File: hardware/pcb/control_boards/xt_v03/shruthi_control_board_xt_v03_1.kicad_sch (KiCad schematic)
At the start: 29 parts, among them IC1 24LC512, IC10 ATMEGA644p, J1 M06SIP, J2 POWER, J3 M03PTH, J4 POWER, Q1 20MHz, U1 AVRISP, X1 MIDI, X2 MIDI

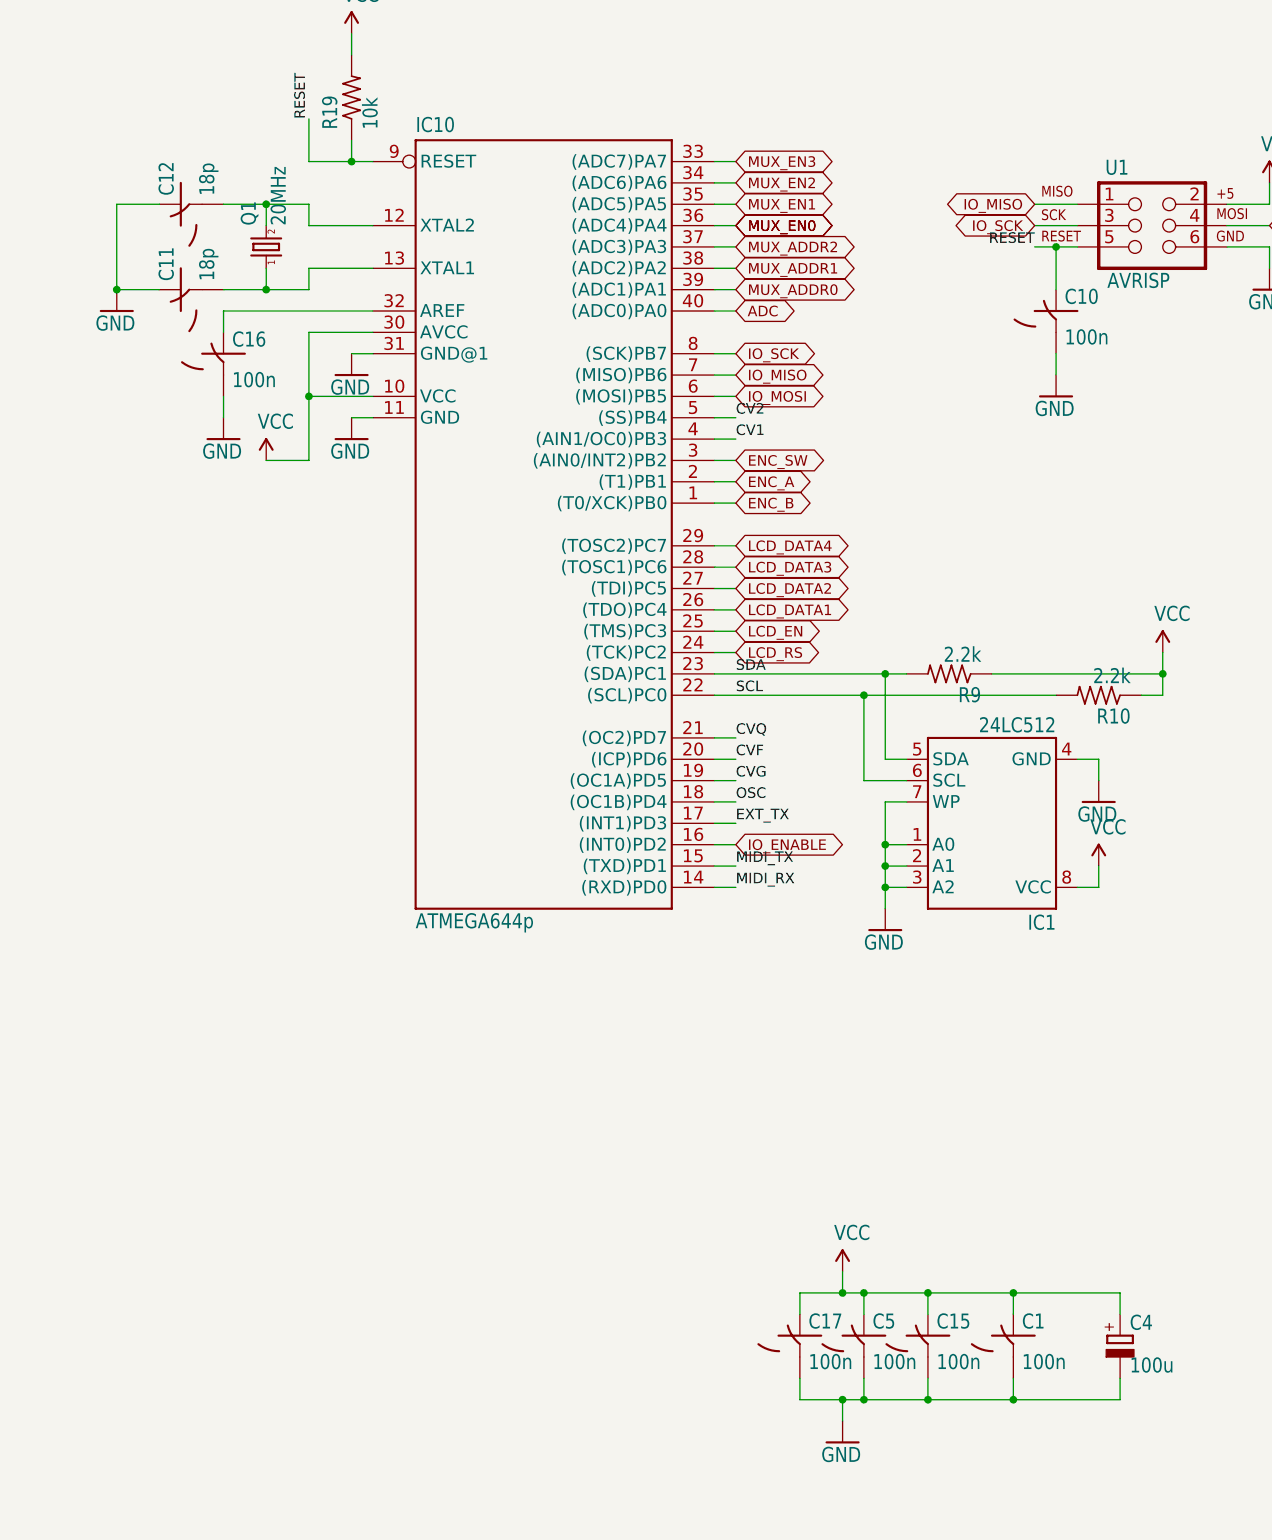
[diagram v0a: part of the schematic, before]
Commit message: update capacitors to use kicad symbols
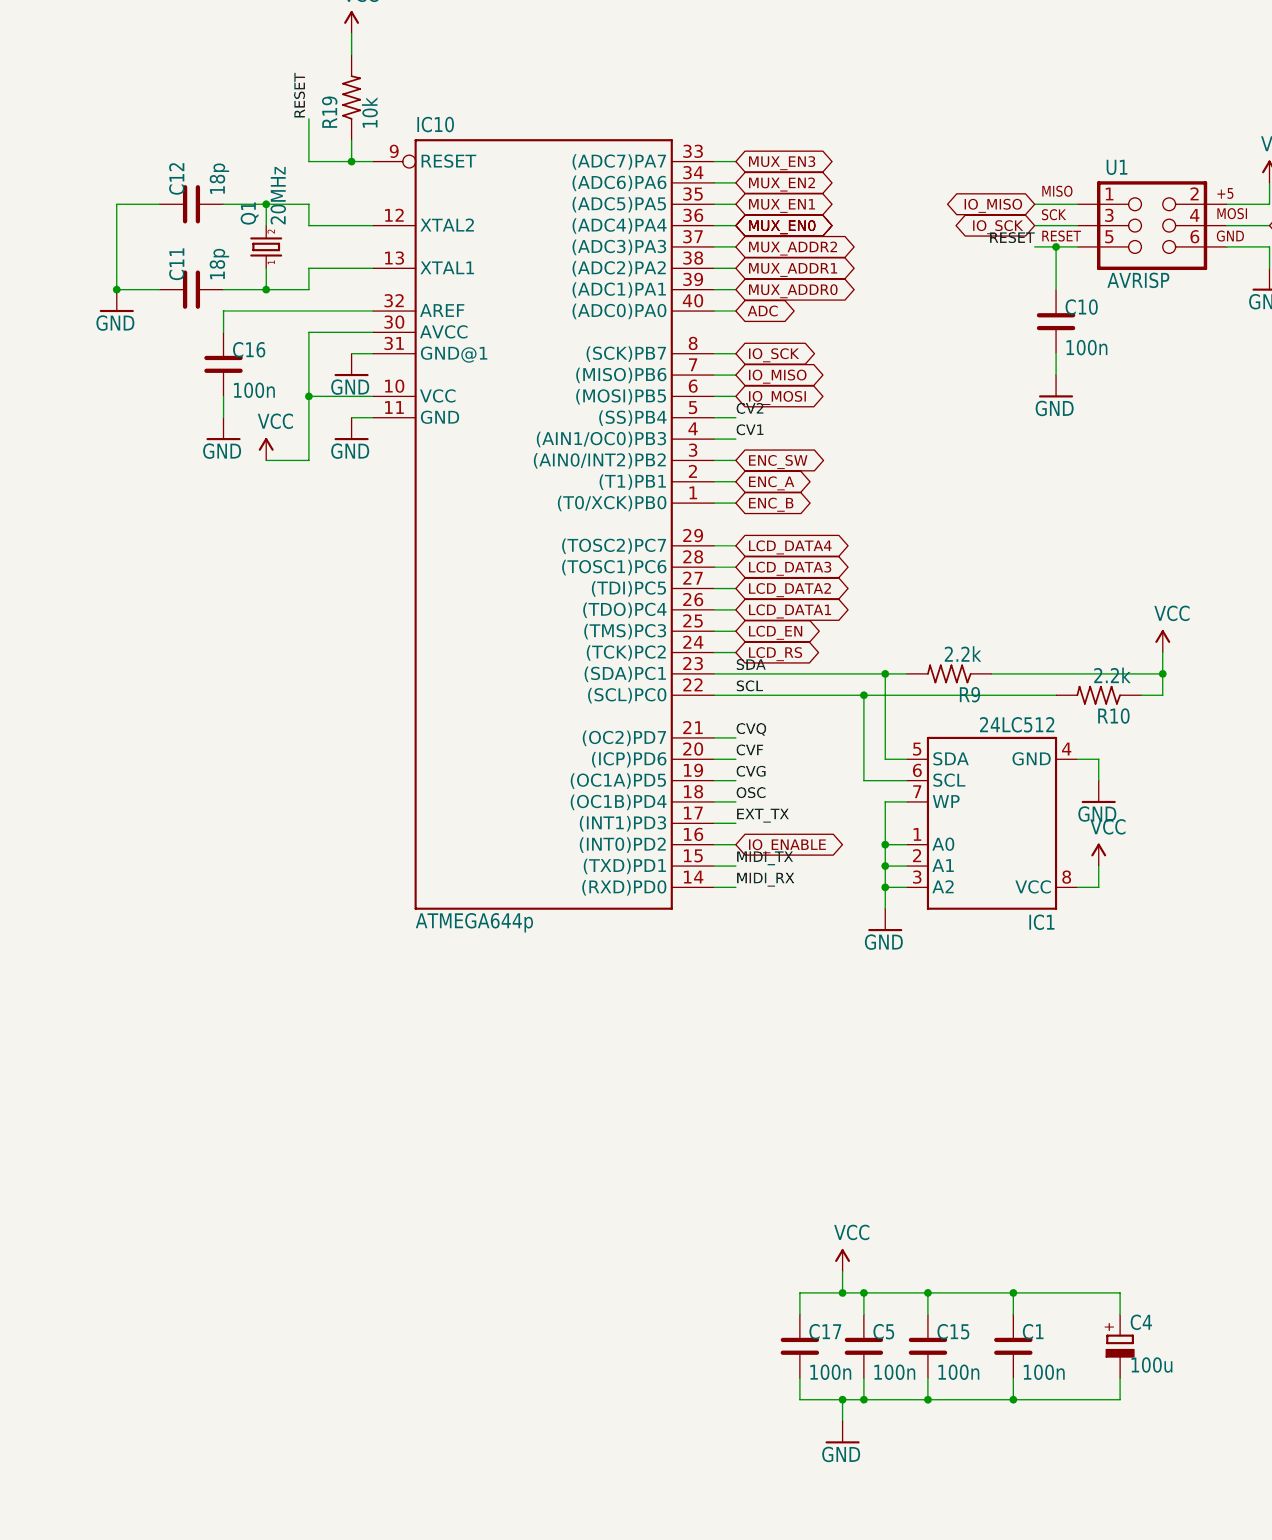
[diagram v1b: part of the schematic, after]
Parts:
- C1, C10, C11, C12, C15, C16, C17, C5: symbol shruthi_control_board_xt_v03-eagle-import:C-US025-024X044 -> Device:C
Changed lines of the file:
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@@
 	)
 	(symbol
-		(lib_id "shruthi_control_board_xt_v03-eagle-import:C-US025-024X044")
-		(at 132.08 116.84 90)
+		(lib_id "Device:C")
+		(at 133.35 116.84 90)
 		(unit 1)
 		(exclude_from_sim no)
@@
 		(dnp no)
 		(property "Reference" "C11"
-			(at 131.445 115.824 0)
+			(at 132.715 115.824 0)
 			(effects
 				(font
@@
 		)
 		(property "Value" "18p"
-			(at 136.271 115.824 0)
+			(at 137.541 115.824 0)
 			(effects
 				(font
@@
 		)
 		(property "Footprint" "shruthi_control_board_xt_v03:C025-024X044"
-			(at 132.08 116.84 0)
+			(at 137.16 115.8748 0)
 			(effects
 				(font
@@
 			)
 		)
-		(property "Datasheet" ""
-			(at 132.08 116.84 0)
+		(property "Datasheet" "~"
+			(at 133.35 116.84 0)
 			(effects
 				(font
@@
 			)
 		)
-		(property "Description" ""
-			(at 132.08 116.84 0)
+		(property "Description" "Unpolarized capacitor"
+			(at 133.35 116.84 0)
 			(effects
 				(font
@@
 	)
 	(symbol
-		(lib_id "shruthi_control_board_xt_v03-eagle-import:C-US025-024X044")
-		(at 137.16 124.46 0)
+		(lib_id "Device:C")
+		(at 137.16 125.73 0)
 		(unit 1)
 		(exclude_from_sim no)
@@
 		(dnp no)
 		(property "Reference" "C16"
-			(at 138.176 123.825 0)
+			(at 138.176 125.095 0)
 			(effects
 				(font
@@
 		)
 		(property "Value" "100n"
-			(at 138.176 128.651 0)
+			(at 138.176 129.921 0)
 			(effects
 				(font
@@
 		)
 		(property "Footprint" "shruthi_control_board_xt_v03:C025-024X044"
-			(at 137.16 124.46 0)
+			(at 138.1252 129.54 0)
 			(effects
 				(font
@@
 			)
 		)
-		(property "Datasheet" ""
-			(at 137.16 124.46 0)
+		(property "Datasheet" "~"
+			(at 137.16 125.73 0)
 			(effects
 				(font
@@
 			)
 		)
-		(property "Description" ""
-			(at 137.16 124.46 0)
+		(property "Description" "Unpolarized capacitor"
+			(at 137.16 125.73 0)
 			(effects
 				(font
@@
 	)
 	(symbol
-		(lib_id "shruthi_control_board_xt_v03-eagle-import:C-US025-024X044")
-		(at 205.74 241.3 0)
+		(lib_id "Device:C")
+		(at 205.74 242.57 0)
 		(unit 1)
 		(exclude_from_sim no)
@@
 		(dnp no)
 		(property "Reference" "C17"
-			(at 206.756 240.665 0)
+			(at 206.756 241.935 0)
 			(effects
 				(font
@@
 		)
 		(property "Value" "100n"
-			(at 206.756 245.491 0)
+			(at 206.756 246.761 0)
 			(effects
 				(font
@@
 		)
 		(property "Footprint" "shruthi_control_board_xt_v03:C025-024X044"
-			(at 205.74 241.3 0)
+			(at 206.7052 246.38 0)
 			(effects
 				(font
@@
 			)
 		)
-		(property "Datasheet" ""
-			(at 205.74 241.3 0)
+		(property "Datasheet" "~"
+			(at 205.74 242.57 0)
 			(effects
 				(font
@@
 			)
 		)
-		(property "Description" ""
-			(at 205.74 241.3 0)
+		(property "Description" "Unpolarized capacitor"
+			(at 205.74 242.57 0)
 			(effects
 				(font
@@
 	)
 	(symbol
-		(lib_id "shruthi_control_board_xt_v03-eagle-import:C-US025-024X044")
-		(at 220.98 241.3 0)
+		(lib_id "Device:C")
+		(at 220.98 242.57 0)
 		(unit 1)
 		(exclude_from_sim no)
@@
 		(dnp no)
 		(property "Reference" "C15"
-			(at 221.996 240.665 0)
+			(at 221.996 241.935 0)
 			(effects
 				(font
@@
 		)
 		(property "Value" "100n"
-			(at 221.996 245.491 0)
+			(at 221.996 246.761 0)
 			(effects
 				(font
@@
 		)
 		(property "Footprint" "shruthi_control_board_xt_v03:C025-024X044"
-			(at 220.98 241.3 0)
+			(at 221.9452 246.38 0)
 			(effects
 				(font
@@
 			)
 		)
-		(property "Datasheet" ""
-			(at 220.98 241.3 0)
+		(property "Datasheet" "~"
+			(at 220.98 242.57 0)
 			(effects
 				(font
@@
 			)
 		)
-		(property "Description" ""
-			(at 220.98 241.3 0)
+		(property "Description" "Unpolarized capacitor"
+			(at 220.98 242.57 0)
 			(effects
 				(font
@@
 	)
 	(symbol
-		(lib_id "shruthi_control_board_xt_v03-eagle-import:C-US025-024X044")
-		(at 236.22 119.38 0)
+		(lib_id "Device:C")
+		(at 236.22 120.65 0)
 		(unit 1)
 		(exclude_from_sim no)
@@
 		(dnp no)
 		(property "Reference" "C10"
-			(at 237.236 118.745 0)
+			(at 237.236 120.015 0)
 			(effects
 				(font
@@
 		)
 		(property "Value" "100n"
-			(at 237.236 123.571 0)
+			(at 237.236 124.841 0)
 			(effects
 				(font
@@
 		)
 		(property "Footprint" "shruthi_control_board_xt_v03:C025-024X044"
-			(at 236.22 119.38 0)
+			(at 237.1852 124.46 0)
 			(effects
 				(font
@@
 			)
 		)
-		(property "Datasheet" ""
-			(at 236.22 119.38 0)
+		(property "Datasheet" "~"
+			(at 236.22 120.65 0)
 			(effects
 				(font
@@
 			)
 		)
-		(property "Description" ""
-			(at 236.22 119.38 0)
+		(property "Description" "Unpolarized capacitor"
+			(at 236.22 120.65 0)
 			(effects
 				(font
@@
 	)
 	(symbol
-		(lib_id "shruthi_control_board_xt_v03-eagle-import:C-US025-024X044")
-		(at 213.36 241.3 0)
+		(lib_id "Device:C")
+		(at 213.36 242.57 0)
 		(unit 1)
 		(exclude_from_sim no)
@@
 		(dnp no)
 		(property "Reference" "C5"
-			(at 214.376 240.665 0)
+			(at 214.376 241.935 0)
 			(effects
 				(font
@@
 		)
 		(property "Value" "100n"
-			(at 214.376 245.491 0)
+			(at 214.376 246.761 0)
 			(effects
 				(font
@@
 		)
 		(property "Footprint" "shruthi_control_board_xt_v03:C025-024X044"
-			(at 213.36 241.3 0)
+			(at 214.3252 246.38 0)
 			(effects
 				(font
@@
 			)
 		)
-		(property "Datasheet" ""
-			(at 213.36 241.3 0)
+		(property "Datasheet" "~"
+			(at 213.36 242.57 0)
 			(effects
 				(font
@@
 			)
 		)
-		(property "Description" ""
-			(at 213.36 241.3 0)
+		(property "Description" "Unpolarized capacitor"
+			(at 213.36 242.57 0)
 			(effects
 				(font
@@
 	)
 	(symbol
-		(lib_id "shruthi_control_board_xt_v03-eagle-import:C-US025-024X044")
-		(at 231.14 241.3 0)
+		(lib_id "Device:C")
+		(at 231.14 242.57 0)
 		(unit 1)
 		(exclude_from_sim no)
@@
 		(dnp no)
 		(property "Reference" "C1"
-			(at 232.156 240.665 0)
+			(at 232.156 241.935 0)
 			(effects
 				(font
@@
 		)
 		(property "Value" "100n"
-			(at 232.156 245.491 0)
+			(at 232.156 246.761 0)
 			(effects
 				(font
@@
 		)
 		(property "Footprint" "shruthi_control_board_xt_v03:C025-024X044"
-			(at 231.14 241.3 0)
+			(at 232.1052 246.38 0)
 			(effects
 				(font
@@
 			)
 		)
-		(property "Datasheet" ""
-			(at 231.14 241.3 0)
+		(property "Datasheet" "~"
+			(at 231.14 242.57 0)
 			(effects
 				(font
@@
 			)
 		)
-		(property "Description" ""
-			(at 231.14 241.3 0)
+		(property "Description" "Unpolarized capacitor"
+			(at 231.14 242.57 0)
 			(effects
 				(font
@@
 	)
 	(symbol
-		(lib_id "shruthi_control_board_xt_v03-eagle-import:C-US025-024X044")
-		(at 132.08 106.68 90)
+		(lib_id "Device:C")
+		(at 133.35 106.68 90)
 		(unit 1)
 		(exclude_from_sim no)
@@
 		(dnp no)
 		(property "Reference" "C12"
-			(at 131.445 105.664 0)
+			(at 132.715 105.664 0)
 			(effects
 				(font
@@
 		)
 		(property "Value" "18p"
-			(at 136.271 105.664 0)
+			(at 137.541 105.664 0)
 			(effects
 				(font
@@
 		)
 		(property "Footprint" "shruthi_control_board_xt_v03:C025-024X044"
-			(at 132.08 106.68 0)
+			(at 137.16 105.7148 0)
 			(effects
 				(font
@@
 			)
 		)
-		(property "Datasheet" ""
-			(at 132.08 106.68 0)
+		(property "Datasheet" "~"
+			(at 133.35 106.68 0)
 			(effects
 				(font
@@
 			)
 		)
-		(property "Description" ""
-			(at 132.08 106.68 0)
+		(property "Description" "Unpolarized capacitor"
+			(at 133.35 106.68 0)
 			(effects
 				(font

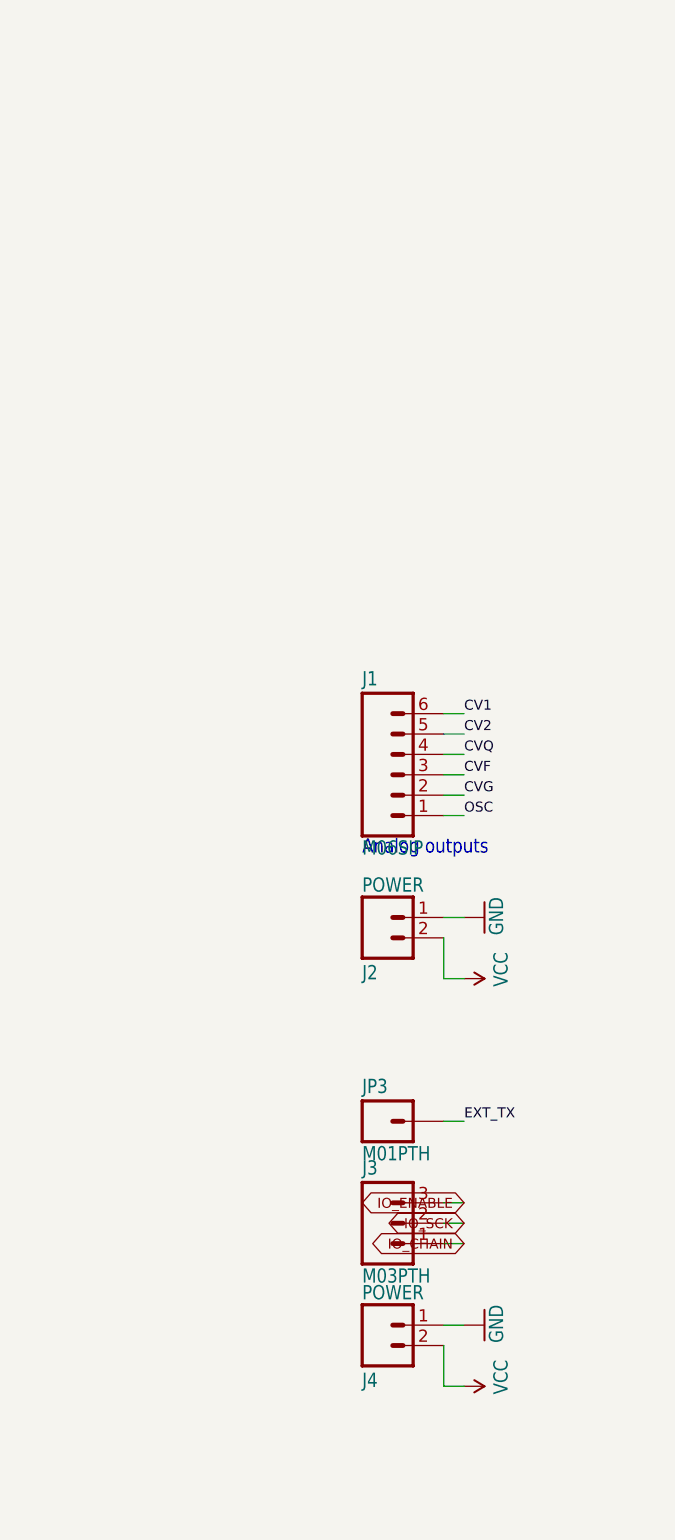
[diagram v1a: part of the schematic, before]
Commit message: update jumpers to use kicad symbols
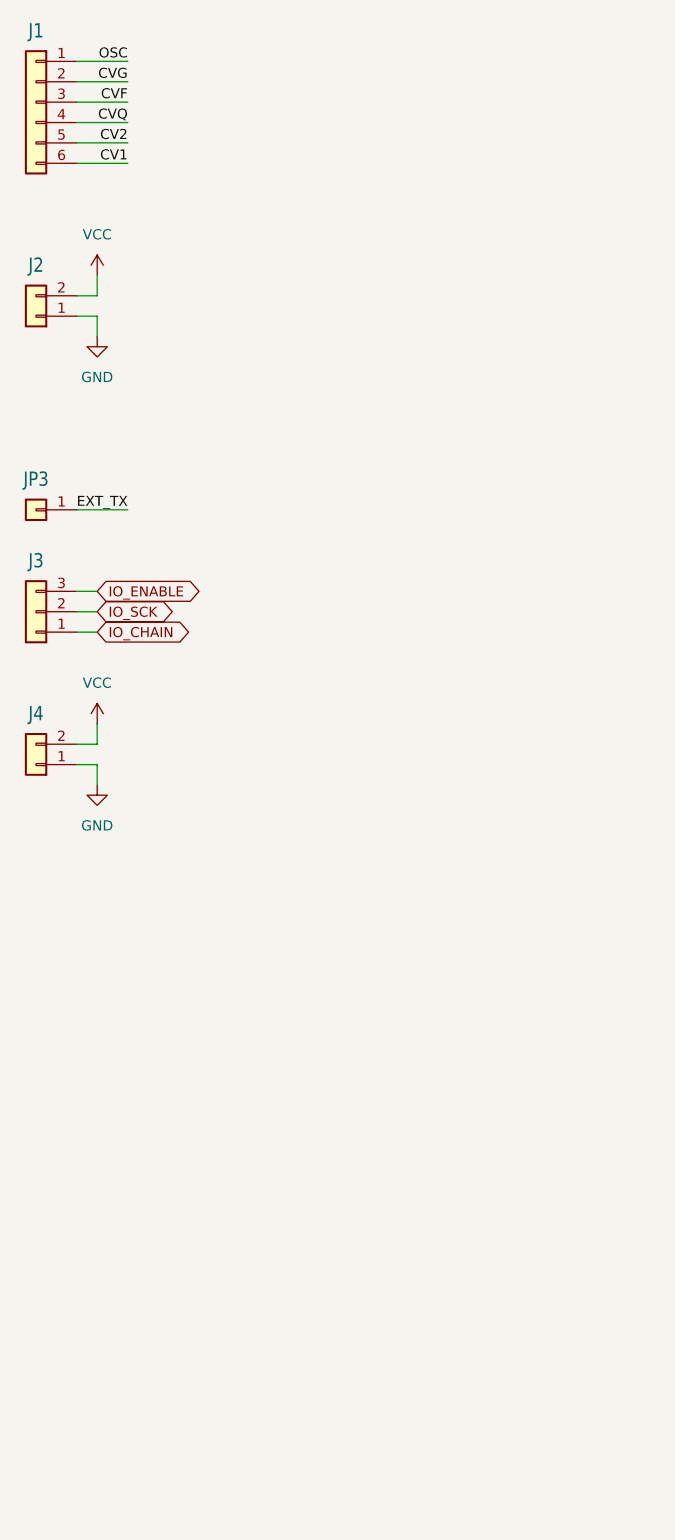
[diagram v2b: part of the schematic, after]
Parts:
- J1: value M06SIP -> CV; symbol shruthi_control_board_xt_v03-eagle-import:M06SIP -> Connector_Generic:Conn_01x06
- J2, J4: symbol shruthi_control_board_xt_v03-eagle-import:M02PTH -> Connector_Generic:Conn_01x02
- J3: symbol shruthi_control_board_xt_v03-eagle-import:M03PTH -> Connector_Generic:Conn_01x03
- JP3: symbol shruthi_control_board_xt_v03-eagle-import:M01PTH -> Connector_Generic:Conn_01x01
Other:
- note removed: "Analog outputs"
